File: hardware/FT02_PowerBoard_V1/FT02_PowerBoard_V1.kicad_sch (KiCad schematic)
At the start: 0 parts

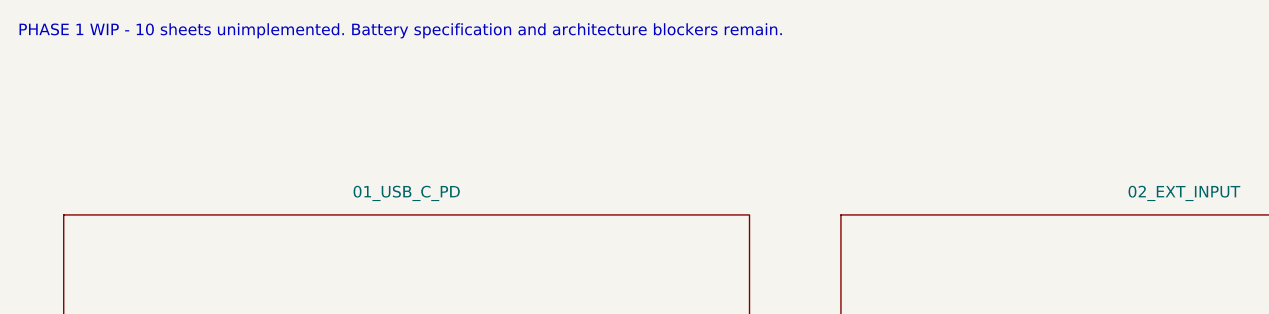
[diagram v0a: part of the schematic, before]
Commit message: 采纳 FT02 电池来源限制并推进 Phase1 电量计参考电路
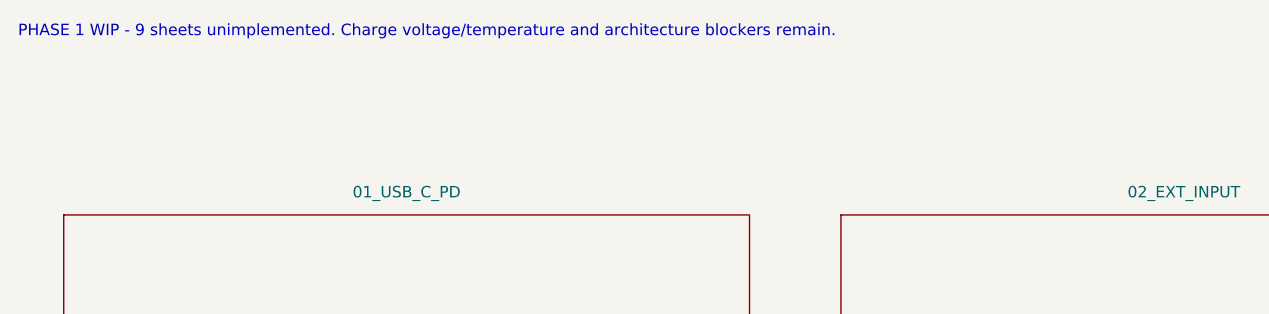
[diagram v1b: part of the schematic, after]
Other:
- note added: "PHASE 1 WIP - 9 sheets unimplemented. Charge voltage/temperature and architecture blockers remain."
- note removed: "PHASE 1 WIP - 10 sheets unimplemented. Battery specification and architecture blockers remain."

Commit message: Wire FT02 Phase 1 power stages and verify partial shunt boundary
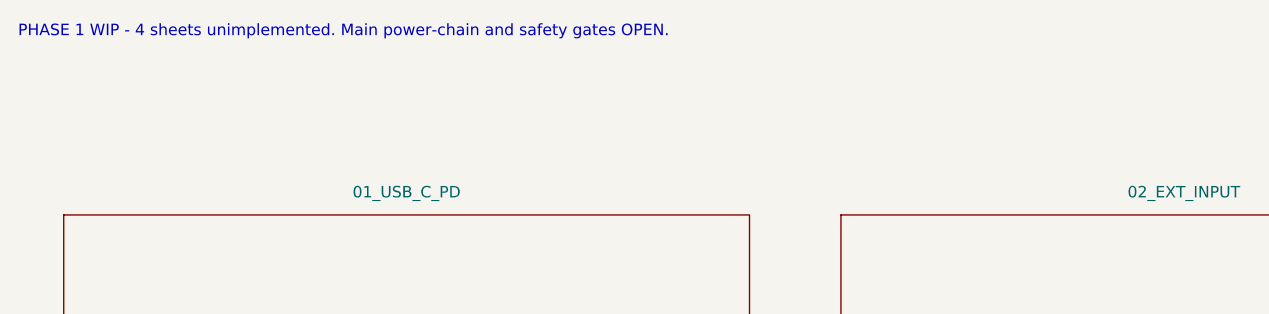
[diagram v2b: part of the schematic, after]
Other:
- note added: "PHASE 1 WIP - 4 sheets unimplemented. Main power-chain and safety gates OPEN."
- note removed: "PHASE 1 WIP - 9 sheets unimplemented. Charge voltage/temperature and architecture blockers remain."

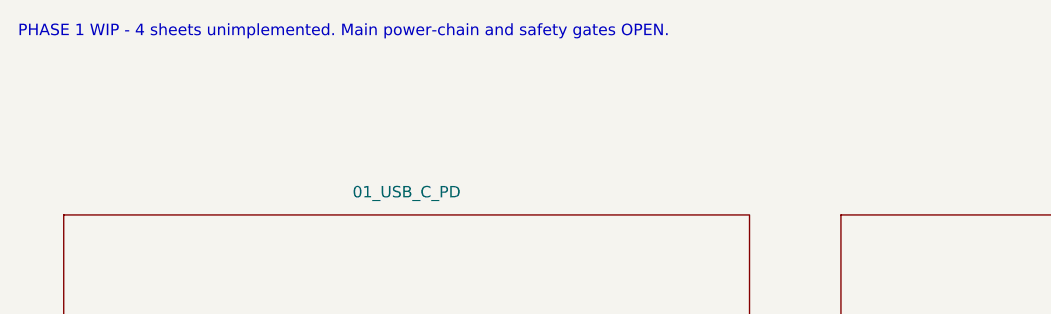
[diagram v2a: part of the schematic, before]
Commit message: Add unqualified FT02 EXT input guard and tolerance checks
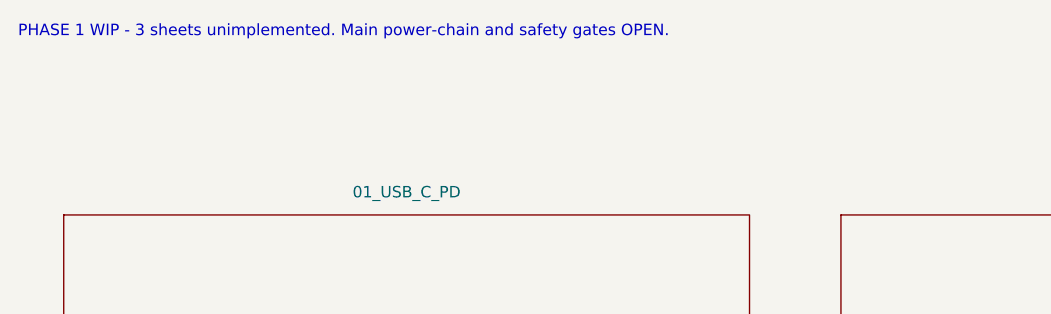
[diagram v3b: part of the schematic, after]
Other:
- note added: "PHASE 1 WIP - 3 sheets unimplemented. Main power-chain and safety gates OPEN."
- note removed: "PHASE 1 WIP - 4 sheets unimplemented. Main power-chain and safety gates OPEN."

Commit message: Wire FT02 mechanical master power gate and audit load unknowns
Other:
- added sheet 13_MASTER_POWER_GATE (13_MASTER_POWER_GATE.kicad_sch)

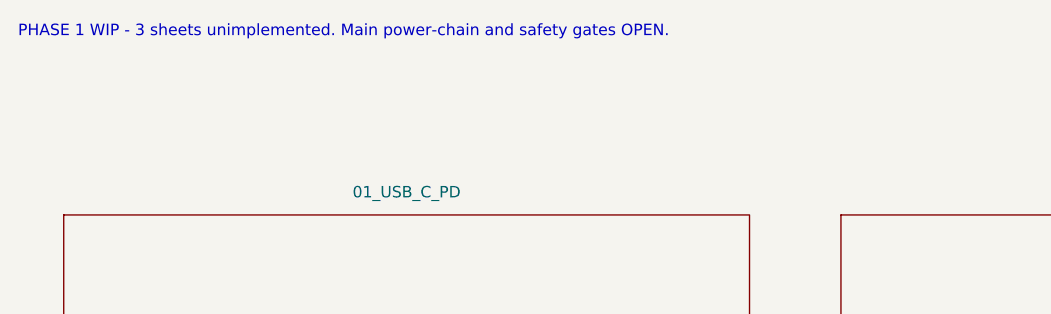
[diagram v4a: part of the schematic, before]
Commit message: Wire FT02 battery guard candidate and export Phase1 review drawings
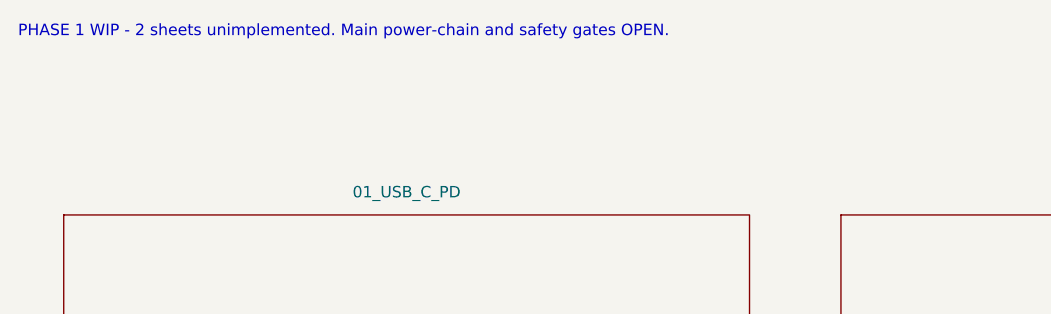
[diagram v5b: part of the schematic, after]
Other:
- note added: "PHASE 1 WIP - 2 sheets unimplemented. Main power-chain and safety gates OPEN."
- note removed: "PHASE 1 WIP - 3 sheets unimplemented. Main power-chain and safety gates OPEN."
